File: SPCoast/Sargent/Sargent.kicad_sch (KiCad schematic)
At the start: 28 parts, among them SW3 1, SW835 835

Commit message: SPCoast: owner's edit: Sargent IRJ B2 becomes IRJ-END_CTC (baseline)
Co-Authored-By: Claude Sonnet 5.5 <noreply@anthropic.com>
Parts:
- removed B2: (no value), symbol Railroad:IRJ
- added B2: END CTC, symbol Railroad:IRJ-END_CTC
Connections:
- net at SW3.1 (C): now also B2.2 (DARK)
- net at B3.2 (B), DOT3.1 (To), TC2.1 (MC): now also B2.1 (CTC)
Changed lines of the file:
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@@
 	)
 	(symbol
-		(lib_id "Railroad:IRJ")
+		(lib_id "Railroad:IRJ-END_CTC")
 		(at 110.49 77.47 0)
 		(unit 1)
@@
 		(fields_autoplaced yes)
 		(property "Reference" "B2"
-			(at 110.49 80.01 0)
+			(at 110.49 84.455 0)
 			(hide yes)
 			(show_name no)
@@
 			)
 		)
-		(property "Value" ""
-			(at 110.49 77.47 0)
-			(hide yes)
+		(property "Value" "END CTC"
+			(at 110.8075 71.12 0)
 			(show_name no)
 			(do_not_autoplace no)
@@
 			)
 		)
-		(property "Description" "Insulated Rail Joint"
+		(property "Description" ""
 			(at 110.49 77.47 0)
 			(hide yes)
@@
 			)
 		)
-		(property "Role" "TRACK"
-			(at 110.49 77.47 0)
+		(property "Kind" "TRACK"
+			(at 110.49 88.265 0)
 			(hide yes)
 			(show_name no)
@@
 			)
 		)
-		(property "Kind" "IRJ"
-			(at 110.49 77.47 0)
+		(property "Role" "END_CTC"
+			(at 110.49 86.36 0)
 			(hide yes)
 			(show_name no)
@@
 			)
 		)
+		(pin "1"
+		)
 		(pin "2"
 		)
-		(pin "1"
-		)
 		(instances

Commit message: SPCoast: owner's edit: END_CTC corrected in library; Corporal B3 and Sargent B2 use IRJ-END_CTC (baseline)
Co-Authored-By: Claude Sonnet 5.5 <noreply@anthropic.com>
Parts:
- B2: Kind TRACK -> END_CTC; Role END_CTC -> TRACK

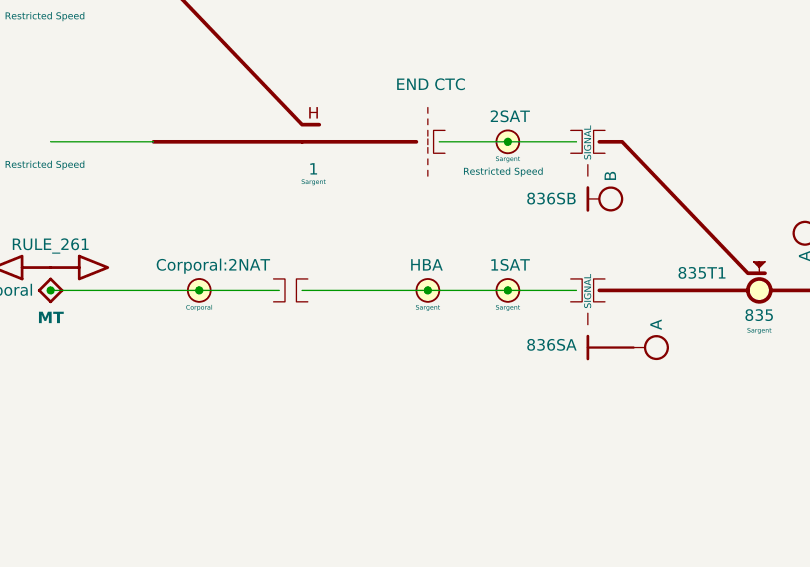
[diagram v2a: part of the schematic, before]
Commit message: SPCoast: owner's edit: Sargent HBA is an AUXILIARY appliance; Watsonville NFLK/SFLK are AUXILIARY_TRAFFIC (baseline)
Co-Authored-By: Claude Sonnet 5.5 <noreply@anthropic.com>
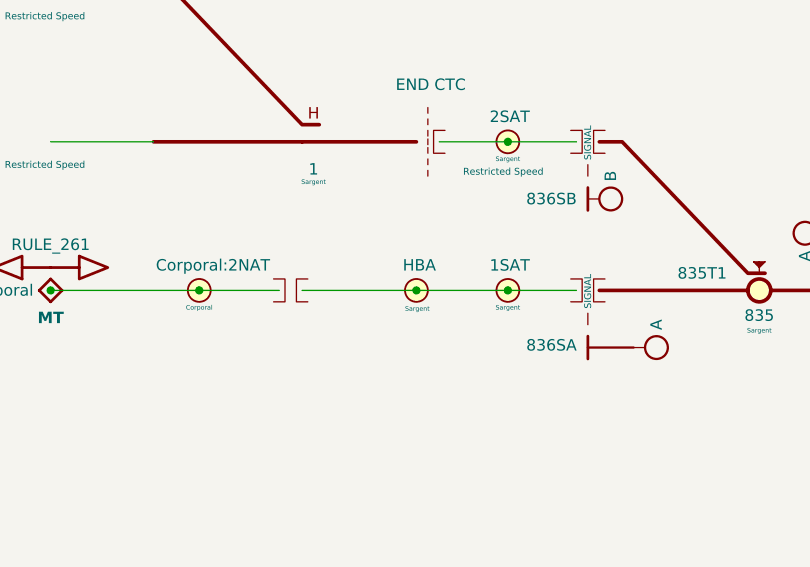
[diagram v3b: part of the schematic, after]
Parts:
- removed TC3: HBA, symbol Railroad:Track Circuit
- added AUX1: HBA, symbol Railroad:AUXILIARY
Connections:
- net at B1.2 (B), B4.2 (B), TC1.1 (MC): now also AUX1.1 (MC)
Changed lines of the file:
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@@
-	)
-	(junction
-		(at 110.49 93.98)
-		(diameter 0)
-		(color 0 0 0 0)
 	)
 	(junction
@@
 	)
 	(junction
+		(at 109.22 93.98)
+		(diameter 0)
+		(color 0 0 0 0)
+	)
+	(junction
 		(at 189.23 93.98)
 		(diameter 0)
@@
 	(wire
 		(pts
-			(xy 110.49 93.98) (xy 119.38 93.98)
+			(xy 96.52 93.98) (xy 109.22 93.98)
 		)
 		(stroke
@@
 		(pts
 			(xy 111.76 77.47) (xy 119.38 77.47)
+		)
+		(stroke
+			(width 0.4064)
+			(type default)
+		)
+	)
+	(wire
+		(pts
+			(xy 109.22 93.98) (xy 119.38 93.98)
 		)
 		(stroke
@@
 		(pts
 			(xy 175.26 93.98) (xy 189.23 93.98)
-		)
-		(stroke
-			(width 0.4064)
-			(type default)
-		)
-	)
-	(wire
-		(pts
-			(xy 96.52 93.98) (xy 110.49 93.98)
 		)
 		(stroke
@@
 	)
 	(symbol
+		(lib_id "Railroad:AUXILIARY")
+		(at 109.22 93.98 0)
+		(unit 1)
+		(body_style 1)
+		(exclude_from_sim no)
+		(in_bom yes)
+		(on_board yes)
+		(in_pos_files yes)
+		(dnp no)
+		(property "Reference" "AUX1"
+			(at 109.22 96.52 0)
+			(hide yes)
+			(show_name no)
+			(do_not_autoplace yes)
+			(effects
+				(font
+					(size 1.27 1.27)
+				)
+			)
+		)
+		(property "Value" "HBA"
+			(at 107.696 91.186 0)
+			(show_name no)
+			(do_not_autoplace no)
+			(effects
+				(font
+					(size 1.27 1.27)
+				)
+				(justify left)
+			)
+		)
+		(property "Footprint" ""
+			(at 109.22 93.98 0)
+			(hide yes)
+			(show_name no)
+			(do_not_autoplace no)
+			(effects
+				(font
+					(size 1.27 1.27)
+				)
+			)
+		)
+		(property "Datasheet" ""
+			(at 109.22 93.98 0)
+			(hide yes)
+			(show_name no)
+			(do_not_autoplace no)
+			(effects
+				(font
+					(size 1.27 1.27)
+				)
+			)
+		)
+		(property "Description" ""
+			(at 109.22 93.98 0)
+			(hide yes)
+			(show_name no)
+			(do_not_autoplace no)
+			(effects
+				(font
+					(size 1.27 1.27)
+				)
+			)
+		)
+		(property "Role" "APPLIANCE"
+			(at 109.22 93.98 0)
+			(hide yes)
+			(show_name no)
+			(do_not_autoplace no)
+			(effects
+				(font
+					(size 1.27 1.27)
+				)
+			)
+		)
+		(property "Kind" "AUXILIARY"
+			(at 109.22 93.98 0)
+			(hide yes)
+			(show_name no)
+			(do_not_autoplace no)
+			(effects
+				(font
+					(size 1.27 1.27)
+				)
+			)
+		)
+		(property "CP" "Sargent"
+			(at 107.95 96.012 0)
+			(show_name no)
+			(do_not_autoplace no)
+			(effects
+				(font
+					(size 0.508 0.508)
+				)
+				(justify left)
+			)
+		)
+		(pin "1"
+		)
+		(instances
+			(project "Sargent"
+				(path "/1c4b404d-a2d2-4d1c-a762-b87ef02fd34f"
+					(reference "AUX1")
+					(unit 1)
+				)
+			)
+		)
+	)
+	(symbol
 		(lib_id "Railroad:IRJ")
 		(at 95.25 93.98 0)
@@
 					(unit 1)
 				)
-			)
-		)
-	)
-	(symbol
-		(lib_id "Railroad:Track Circuit")
-		(at 110.49 93.98 0)
-		(unit 1)
-		(body_style 1)
-		(exclude_from_sim no)
-		(in_bom yes)
-		(on_board yes)
-		(in_pos_files yes)
-		(dnp no)
-		(property "Reference" "TC3"
-			(at 110.49 89.54 0)
-			(hide yes)
-			(show_name no)
-			(do_not_autoplace no)
-			(effects
-				(font
-					(size 1.27 1.27)
-				)
-			)
-		)
-		(property "Value" "HBA"
-			(at 108.46 91.19 0)
-			(show_name no)
-			(do_not_autoplace no)
-			(effects
-				(font
-					(size 1.27 1.27)
-				)
-				(justify left)
-			)
-		)
-		(property "Footprint" ""
-			(at 110.49 93.98 0)
-			(hide yes)
-			(show_name no)
-			(do_not_autoplace no)
-			(effects
-				(font
-					(size 1.27 1.27)
-				)
-			)
-		)
-		(property "Datasheet" ""
-			(at 110.49 93.98 0)
-			(hide yes)
-			(show_name no)
-			(do_not_autoplace no)
-			(effects
-				(font
-					(size 1.27 1.27)
-				)
-			)
-		)
-		(property "Description" ""
-			(at 110.49 93.98 0)
-			(hide yes)
-			(show_name no)
-			(do_not_autoplace no)
-			(effects
-				(font
-					(size 1.27 1.27)
-				)
-			)
-		)
-		(property "CP" "Sargent"
-			(at 110.49 95.88 0)
-			(show_name no)
-			(do_not_autoplace no)
-			(effects
-				(font
-					(size 0.508 0.508)
-					(color 72 72 72 1)
-				)
-			)
-		)
-		(property "Role" "APPLIANCE"
-			(at 110.49 93.98 0)
-			(hide yes)
-			(show_name no)
-			(do_not_autoplace no)
-			(effects
-				(font
-					(size 1.27 1.27)
-				)
-			)
-		)
-		(property "Kind" "TRACK_CIRCUIT"
-			(at 110.49 93.98 0)
-			(hide yes)
-			(show_name no)
-			(do_not_autoplace no)
-			(effects
-				(font
-					(size 1.27 1.27)
-				)
-			)
-		)
-		(pin "1"
-		)
-		(instances
-			(project "Sargent"
-				(path "/1c4b404d-a2d2-4d1c-a762-b87ef02fd34f"
-					(reference "TC3")
-					(unit 1)
-				)

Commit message: SPCoast: owner's edits: schematics synced with the revised symbol libraries (baseline)
Update Symbols from Library on all plant and desk sheets; CP values for
Christopher, GilroyInterchange and Luchessa; Restricted Speed markers
consolidated in Corporal, Luchessa and Sargent.

Observed in the diff, not changed by the sweep that follows: CP changed on 23
symbols (Christopher: prefix removed, 815/815A/IND now Christopher North) and
added on 12 (GilroyInterchange); two lamps' Color reset to their symbol variant
(Christopher LMP93 red -> yellow, Sargent LMP133 yellow -> red).

Verified: netlists keep their net counts (Christopher 33, Corporal 26,
GilroyCalTrain 27, GilroyInterchange 22, Luchessa 34, Sargent 18, Watsonville
96, South-cTc 341); desk compiles to 75 appliances, 137 bindings, 14 columns;
no root-UUID regression.

Co-Authored-By: Claude Sonnet 5.5 <noreply@anthropic.com>
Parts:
- removed DOT1, DOT2, DOT3: Restricted Speed, symbol Railroad:Rule105-RestrictedSpeed
- added DOT6: Restricted Speed, symbol Railroad:Rule105-RestrictedSpeed
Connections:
- net at B2.1 (CTC), B3.2 (B), TC2.1 (TC): now also DOT6.1 (To)

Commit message: chore(kicad): sweep instance Role/Kind and stale fields to the library vocabulary
Scripted, one pass over every sheet except Watsonville (open in KiCad, locked):
- Role/Kind of placed symbols refreshed from the library by lib_id: 10 Role
  (MAIN HOUSE CONTROLLED_POINT -> CONTROL_POINT, Rule251-DoT empty) and 17 Kind
  (IRJ-Signal IRJ -> IRJ_SIGNAL x7, Mast_Single/Double swaps, HandThrow
  -> SWITCH_MANUAL, Derail, PanelLock -> LOCK_LEVER, NextCP).
- Stale instance fields dropped where the library no longer has them: 39 Name,
  28 Direction (all empty or retired), 5 CP on Bumper and IRJ symbols.
- Orphan embedded copies of the retired symbol Rule6.28-OtherThanMain removed
  from two sheets (unused).

Not done: Watsonville (locked); CMRInet -> CMRI (library Kind still CMRInet);
fields new to the library (MAIN HOUSE Kind, switch Indications) are not copied
onto instances, the compiler will read library defaults by lib_id; Rulebook
fields stay until the compiler stops requiring them.

Verified: per-symbol before/after comparison shows only these changes, same
symbol sets, positions and lib_ids; netlists keep their net counts (Christopher
33, Corporal 26, GilroyCalTrain 27, GilroyInterchange 22, Luchessa 34, Sargent
18, South-cTc 341); desk still 75 appliances, 137 bindings, 14 columns.

Co-Authored-By: Claude Sonnet 5.5 <noreply@anthropic.com>
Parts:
- HOUSE1: Role CONTROLLED_POINT -> CONTROL_POINT
- SW3: Kind SWITCH_POWERED -> SWITCH_MANUAL
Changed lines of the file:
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@@
 			)
 		)
-		(property "Kind" "SWITCH_POWERED"
+		(property "Kind" "SWITCH_MANUAL"
 			(at 97.79 77.47 0)
 			(hide yes)
@@
 			)
 		)
-		(property "Role" "CONTROLLED_POINT"
+		(property "Role" "CONTROL_POINT"
 			(at 147.32 46.99 0)
 			(hide yes)

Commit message: chore(kicad): masts and maintainer calls carry no CP; IRJ-Signals do; CMRInet Kind is CMRI
Owner decision: an IRJ-Signal is the single source of a signal's control point
(a mast attaches to exactly one IRJ-Signal through its SIGNAL pin); a
maintainer call is tied to its house by the netlist.
- CP dropped from 23 masts and 5 maintainer calls.
- 7 empty IRJ-Signal CPs filled with the plant's only house (Corporal, Sargent).
- 43 empty Name fields that KiCad re-added to Christopher dropped again.
- Codeline-Transport Kind CMRInet -> CMRI on the placed instance and the
  embedded library copy (South-cTc root sheet).

Verified: per-symbol before/after comparison shows only these changes; every
IRJ-Signal in all seven plants has a CP naming one of its plant's houses; net
counts unchanged (Christopher 33, Corporal 26, GilroyCalTrain 27,
GilroyInterchange 22, Luchessa 34, Sargent 18, Watsonville 96, South-cTc 341);
desk compiles to 75 appliances, 137 bindings, 14 columns. Remaining CP
diagnostic: Sargent's Corporal:2NAT placeholder (cross-plant reference).

Co-Authored-By: Claude Sonnet 5.5 <noreply@anthropic.com>
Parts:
- B3, B4, B5: CP (none) -> Sargent
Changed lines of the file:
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@@
 			)
 		)
-		(property "CP" ""
+		(property "CP" "Sargent"
 			(at 158.115 92.075 0)
 			(show_name no)
@@
 			)
 		)
-		(property "CP" ""
+		(property "CP" "Sargent"
 			(at 130.175 95.885 0)
 			(show_name no)
@@
 			)
 		)
-		(property "CP" ""
+		(property "CP" "Sargent"
 			(at 130.175 79.375 0)
 			(show_name no)

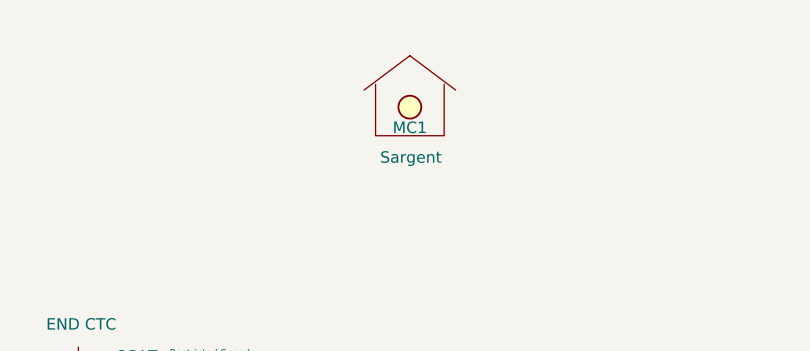
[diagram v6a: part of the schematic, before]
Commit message: SPCoast: owner's edits: Interlocking symbol on every Trackplan; MAIN HOUSE is STRUCTURE/CONTROL_POINT (baseline)
Each plant has one Interlocking symbol (Value is the authoritative name) and
every MAIN HOUSE's Interlocking pin is wired to it. Library Role/Kind:
Interlocking is STRUCTURE/INTERLOCKING, MAIN HOUSE is STRUCTURE/CONTROL_POINT
(refreshed on all instances by the owner).

Verified: one Interlocking symbol per plant; every house shares a net with it;
net counts are one higher than before in each plant (Christopher 34, Corporal
27, GilroyCalTrain 28, GilroyInterchange 23, Luchessa 35, Sargent 19,
Watsonville 97); no root-UUID regression; no symbol moved or removed.

Co-Authored-By: Claude Sonnet 5.5 <noreply@anthropic.com>
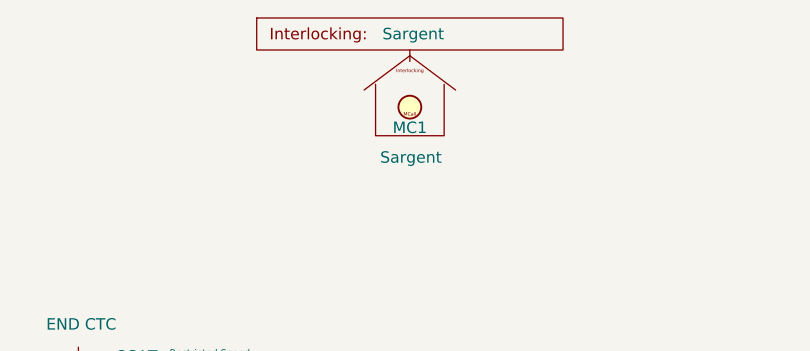
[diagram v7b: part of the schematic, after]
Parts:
- added Plant1: ${TITLE}, symbol Railroad:Interlocking
- HOUSE1: Kind (none) -> CONTROL_POINT; Role CONTROL_POINT -> STRUCTURE
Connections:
- new net: HOUSE1.2 (Interlocking), Plant1.1 (Interlocking)
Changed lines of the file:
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@@
 			)
 		)
-		(property "Description" "Rrepresents the Control Point Maintainer Bungalow (plus optional Maintainer Call)"
+		(property "Description" "The Control Point Maintainer Bungalow (plus optional Maintainer Call)"
 			(at 147.32 52.705 0)
 			(hide yes)
@@
 			)
 		)
-		(property "Role" "CONTROL_POINT"
-			(at 147.32 46.99 0)
+		(property "Role" "STRUCTURE"
+			(at 132.08 44.45 0)
+			(hide yes)
+			(show_name no)
+			(do_not_autoplace no)
+			(effects
+				(font
+					(size 1.27 1.27)
+				)
+			)
+		)
+		(property "Kind" "CONTROL_POINT"
+			(at 133.985 46.482 0)
 			(hide yes)
 			(show_name no)
@@
 		)
 		(pin "1"
+		)
+		(pin "2"
 		)
 		(instances
@@
 					(unit 1)
 				)
+			)
+		)
+	)
+	(symbol
+		(lib_id "Railroad:Interlocking")
+		(at 147.32 41.91 0)
+		(unit 1)
+		(body_style 1)
+		(exclude_from_sim no)
+		(in_bom yes)
+		(on_board yes)
+		(in_pos_files yes)
+		(dnp no)
+		(fields_autoplaced yes)
+		(property "Reference" "Plant1"
+			(at 133.096 36.068 0)
+			(hide yes)
+			(show_name no)
+			(do_not_autoplace no)
+			(effects
+				(font
+					(size 1.27 1.27)
+				)
+			)
+		)
+		(property "Value" "${TITLE}"
+			(at 144.272 38.862 0)
+			(show_name no)
+			(do_not_autoplace yes)
+			(effects
+				(font
+					(size 1.27 1.27)
+				)
+				(justify left)
+			)
+		)
+		(property "Footprint" ""
+			(at 147.32 41.91 0)
+			(hide yes)
+			(show_name no)
+			(do_not_autoplace no)
+			(effects
+				(font
+					(size 1.27 1.27)
+				)
+			)
+		)
+		(property "Datasheet" ""
+			(at 147.32 41.91 0)
+			(hide yes)
+			(show_name no)
+			(do_not_autoplace no)
+			(effects
+				(font
+					(size 1.27 1.27)
+				)
+			)
+		)
+		(property "Description" ""
+			(at 147.32 41.91 0)
+			(hide yes)
+			(show_name no)
+			(do_not_autoplace no)
+			(effects
+				(font
+					(size 1.27 1.27)
+				)
+			)
+		)
+		(property "Role" "STRUCTURE"
+			(at 136.017 32.258 0)
+			(hide yes)
+			(show_name no)
+			(do_not_autoplace no)
+			(effects
+				(font
+					(size 1.27 1.27)
+				)
+			)
+		)
+		(property "Kind" "INTERLOCKING"
+			(at 137.414 33.909 0)
+			(hide yes)
+			(show_name no)
+			(do_not_autoplace no)
+			(effects
+				(font
+					(size 1.27 1.27)
+				)
+			)
+		)
+		(pin "1"
+		)
+		(instances
+			(project "Sargent"
+				(path "/1c4b404d-a2d2-4d1c-a762-b87ef02fd34f"
+					(reference "Plant1")
+					(unit 1)
+				)

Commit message: SPCoast: owner's edits: NextCP names, Christopher heads and masts, Sargent milepost, Watsonville circuits and desk tokens (baseline)
- NextCP values name interlockings: GilroyCalTrain CP2 -> Gilroy Interchange;
  Luchessa CP1 -> Gilroy Interchange, CP2 -> Hollister, CP3 and CP4 ->
  Christopher.
- Christopher: the two unnamed dwarf masts, their IRJ-Signals (now plain IRJs)
  and heads removed; remaining heads lettered A, B, C.
- Sargent MAIN HOUSE Milepost 83.5.
- Watsonville circuits SDT -> 0DT and SAT -> 0AT; desk tokens 0DT, 0AT, AT and
  Watsonville:837T1 follow.

Verified: netlists rebuild (Christopher 30, Corporal 27, GilroyCalTrain 28,
GilroyInterchange 23, Luchessa 35, Sargent 19, Watsonville 97, South-cTc 341);
Christopher has no mast or head diagnostics left; desk compiles to 75
appliances, 137 bindings, 14 columns; no root-UUID regression.

Co-Authored-By: Claude Sonnet 5.5 <noreply@anthropic.com>
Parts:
- HOUSE1: Milepost FIXME -> 83.5
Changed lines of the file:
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@@
 			)
 		)
-		(property "Milepost" "FIXME"
+		(property "Milepost" "83.5"
 			(at 147.32 52.71 0)
 			(hide yes)
